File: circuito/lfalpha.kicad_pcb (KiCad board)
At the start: 2 copper layers, 200 x 100 mm, 48 parts, among them J1 BAT, J2 ANALOG, J3 MotorA, J4 MotorB, J5 Bluetooth, J6 REMOTE S/S, J7 SPI, J8 SENSOR CON, J9 SENSOR BAR, SW1 ON/OFF, SW2 START, SW3 STOP, U1 AruinoNano, U2 DRV8835-Carrier, U3 QRE1113, U4 QRE1113, U5 QRE1113, U6 QRE1113, U7 QRE1113, U8 QRE1113

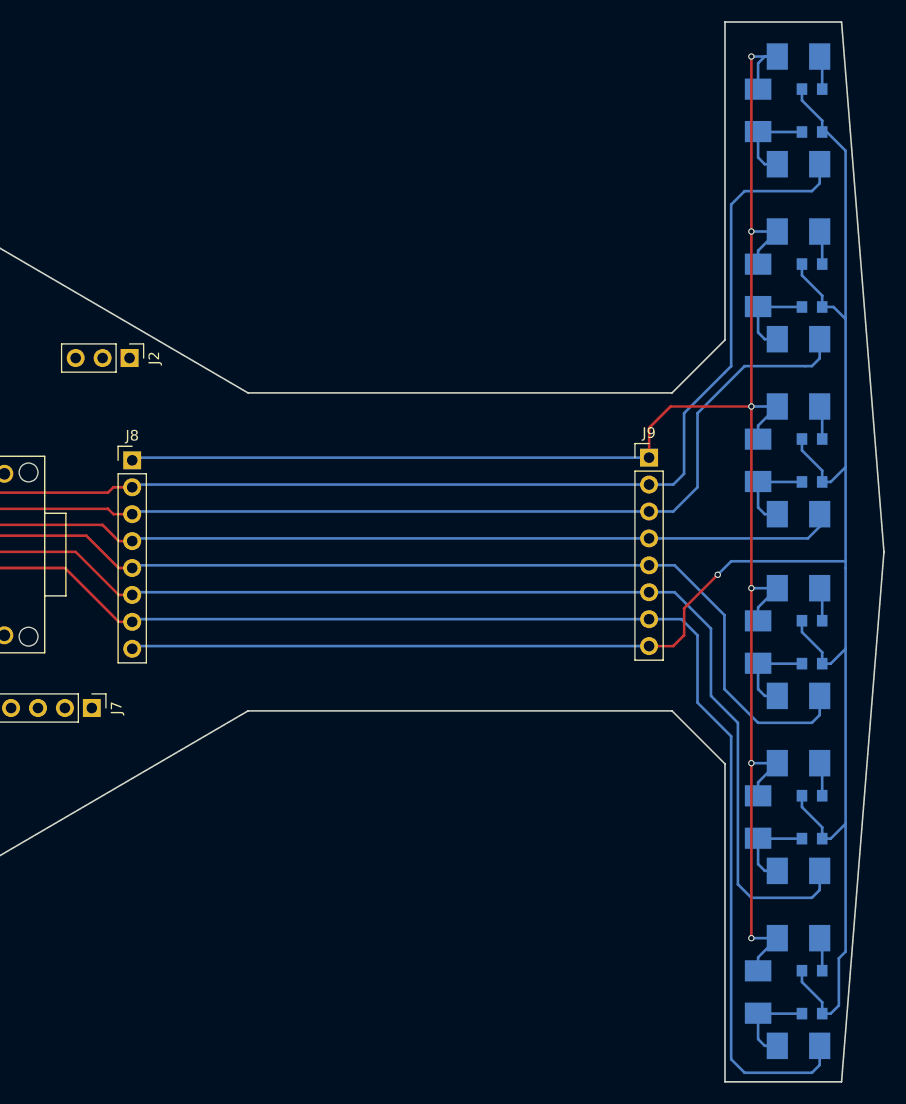
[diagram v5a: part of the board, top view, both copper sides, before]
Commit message: Aggiunto un nuovo Roles per le piste associato alla parte di alimentazione, e ridisegnate alcune piste della barra sensori, ma da completare. Creta l'asola per il ruotino.
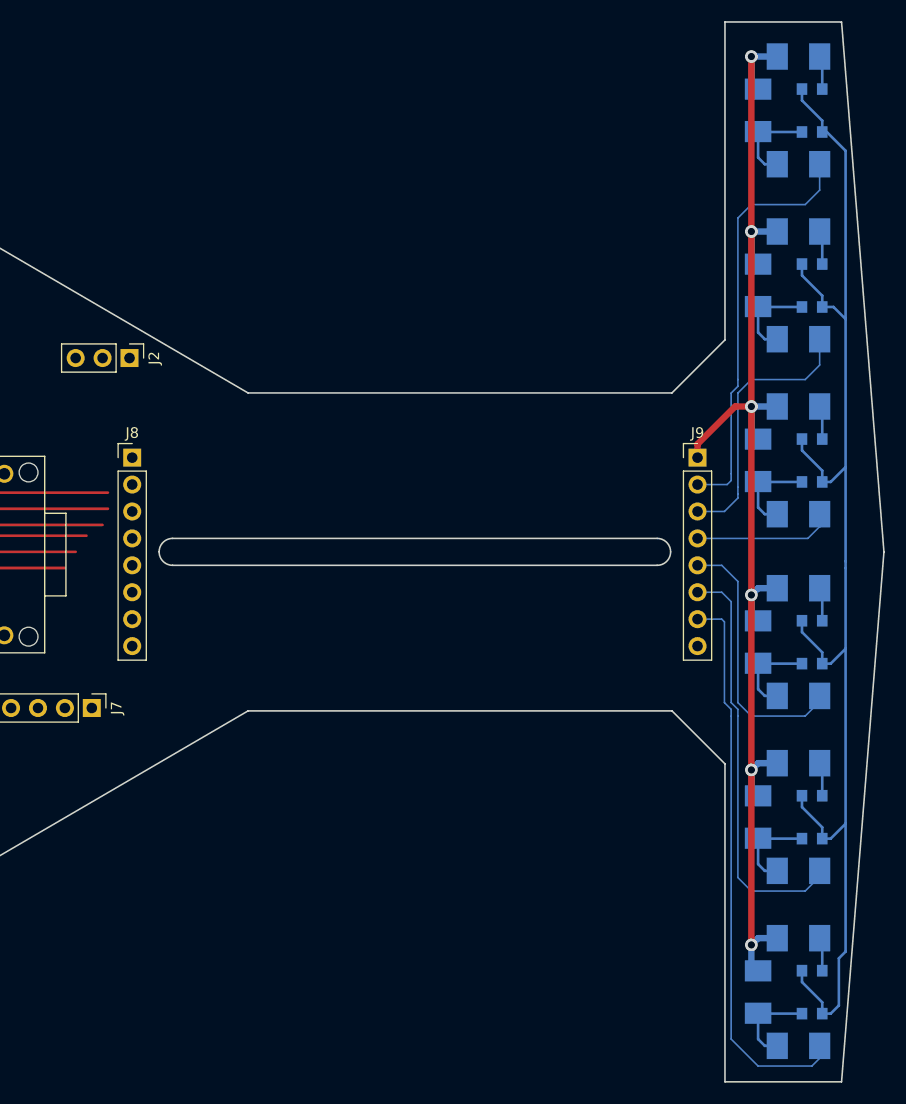
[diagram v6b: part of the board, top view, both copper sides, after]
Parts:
- moved J9 4.57 mm to (232.4, 86.1)
- moved J8 0.25 mm to (179.1, 86.1)
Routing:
- net GND: track 197.7 -> 125.8 mm, vias 1 -> 0
- net Net-(J8-Pad7): track 148.7 -> 87.4 mm
- net Net-(J8-Pad6): track 129.5 -> 70.4 mm
- net +5V: track 183.3 -> 125.3 mm
- net Net-(J8-Pad5): track 110.4 -> 53.1 mm
- net Net-(J8-Pad4): track 95.8 -> 40.5 mm
- net Net-(J8-Pad3): track 101.6 -> 48.1 mm
- net Net-(J8-Pad2): track 111.8 -> 58.4 mm
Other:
- outline, holes or cut-outs redrawn
- net class Alimentazione added: clearance 0.3048, trace_width 0.6096, via_dia 1.1938, via_drill 0.6858

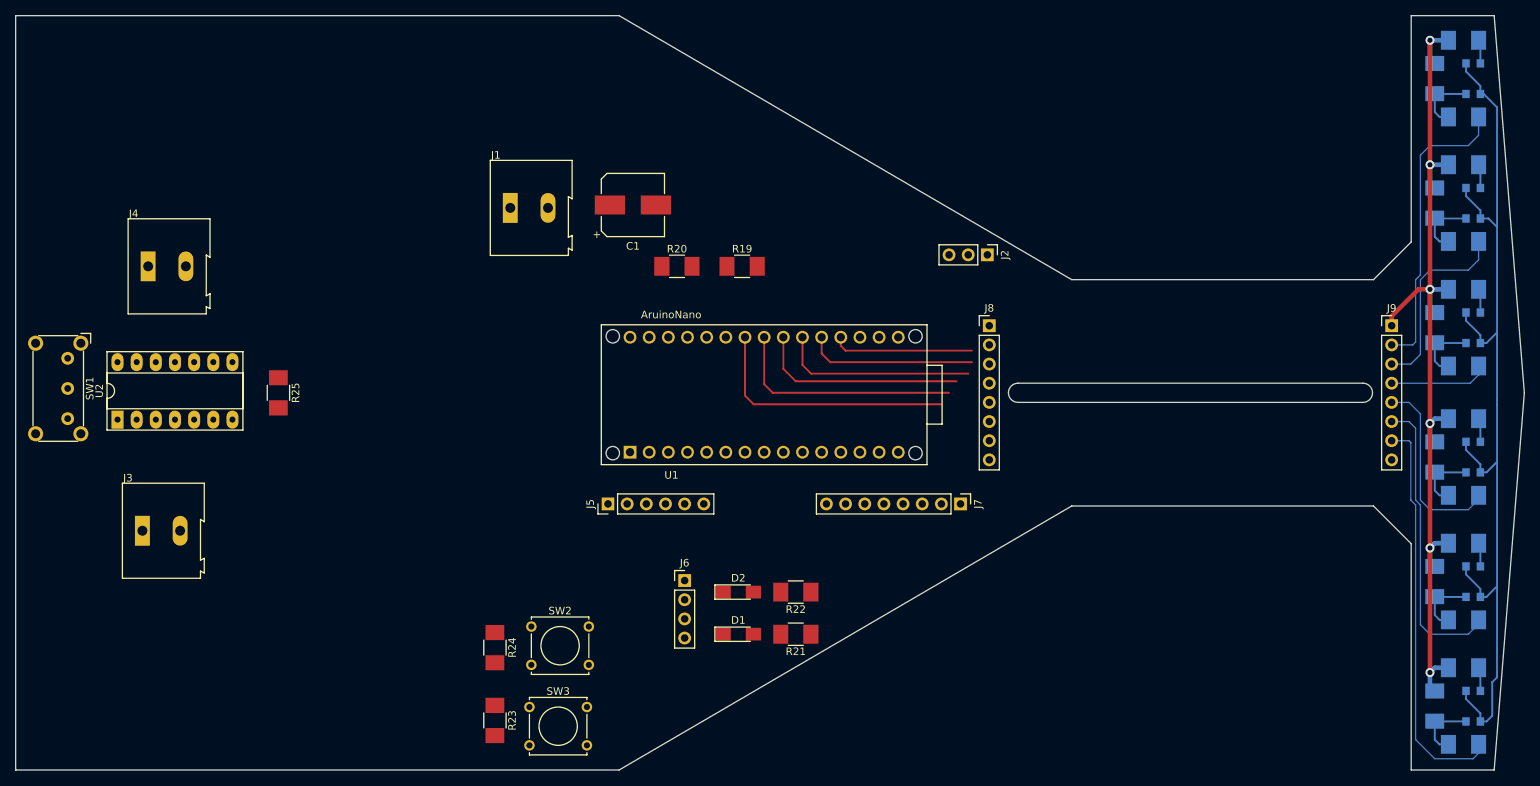
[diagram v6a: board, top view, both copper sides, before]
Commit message: Completate le interconessioni con i sensori e Arduino, piazzati i mount hole per eventuali tagli della barra. Verificare se e come si possono cambiare i connettori attualmente posizionati sulla vista 3D, con altri a 90°
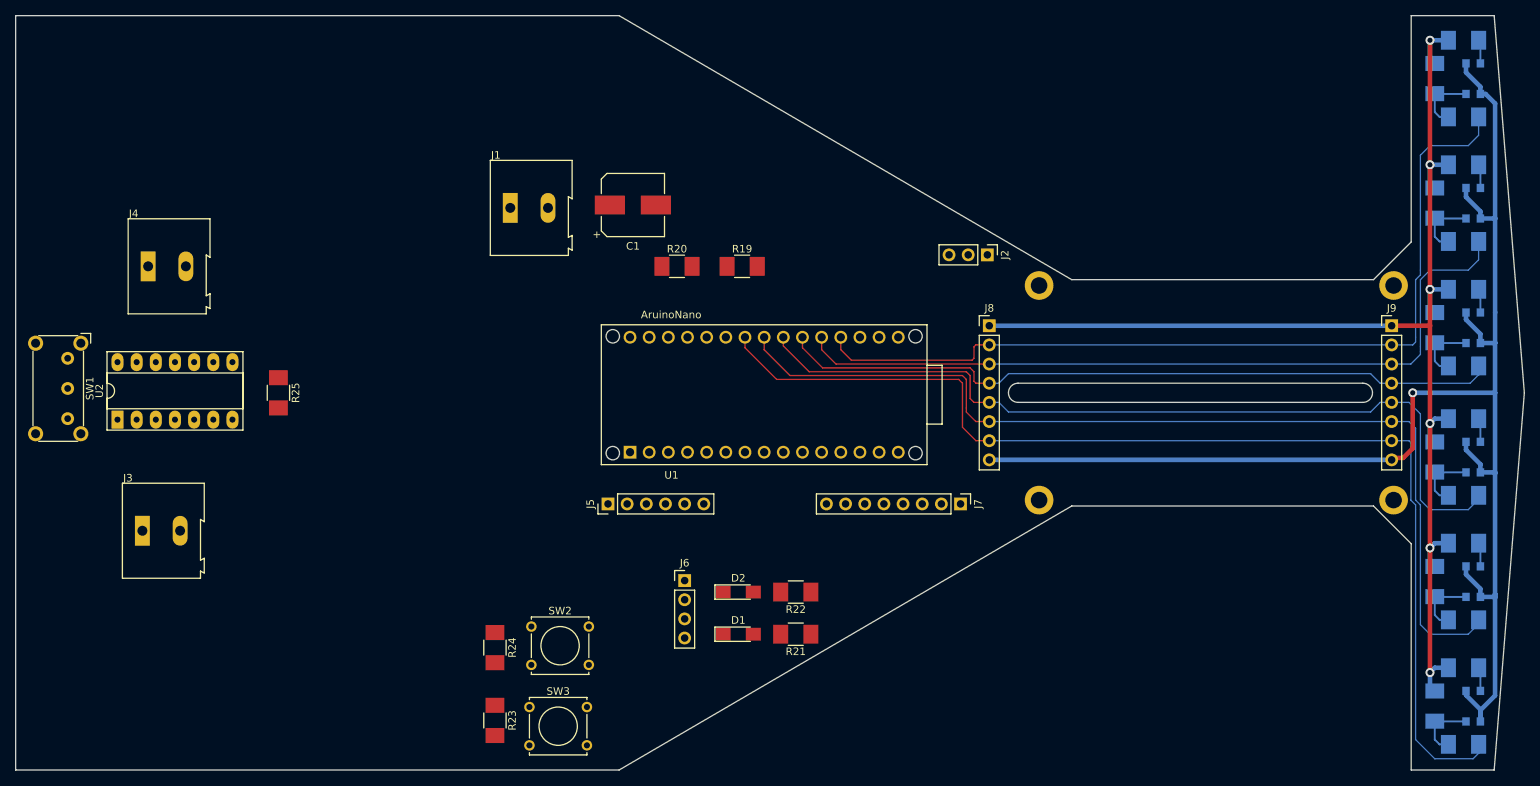
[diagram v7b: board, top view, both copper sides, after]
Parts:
- added REF**: MountingHole_2.2mm_M2_DIN965_Pad, Mounting_Holes:MountingHole_2.2mm_M2_DIN965_Pad, F.Cu at (232.7, 80.8)
- added REF**: MountingHole_2.2mm_M2_DIN965_Pad, Mounting_Holes:MountingHole_2.2mm_M2_DIN965_Pad, F.Cu at (232.7, 109.2)
- added REF**: MountingHole_2.2mm_M2_DIN965_Pad, Mounting_Holes:MountingHole_2.2mm_M2_DIN965_Pad, F.Cu at (185.7, 80.8)
- added REF**: MountingHole_2.2mm_M2_DIN965_Pad, Mounting_Holes:MountingHole_2.2mm_M2_DIN965_Pad, F.Cu at (185.7, 109.2)
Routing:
- net GND: track 125.8 -> 198.3 mm, vias 0 -> 1
- net Net-(J8-Pad7): track 87.4 -> 148.8 mm
- net Net-(J8-Pad6): track 70.4 -> 130.5 mm
- net Net-(J8-Pad5): track 53.1 -> 112.9 mm
- net Net-(J8-Pad2): track 58.4 -> 116.6 mm
- net Net-(J8-Pad4): track 40.5 -> 97.6 mm
- net Net-(J8-Pad3): track 48.1 -> 103.5 mm
- net +5V: track 125.3 -> 175.9 mm

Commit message: Cambiati i connettori strip per avere meno connettori di forma diversa, sistemati alcuni collegamenti per agevolare lo sbroglio. Ridistribuiti connettori e driver motori.
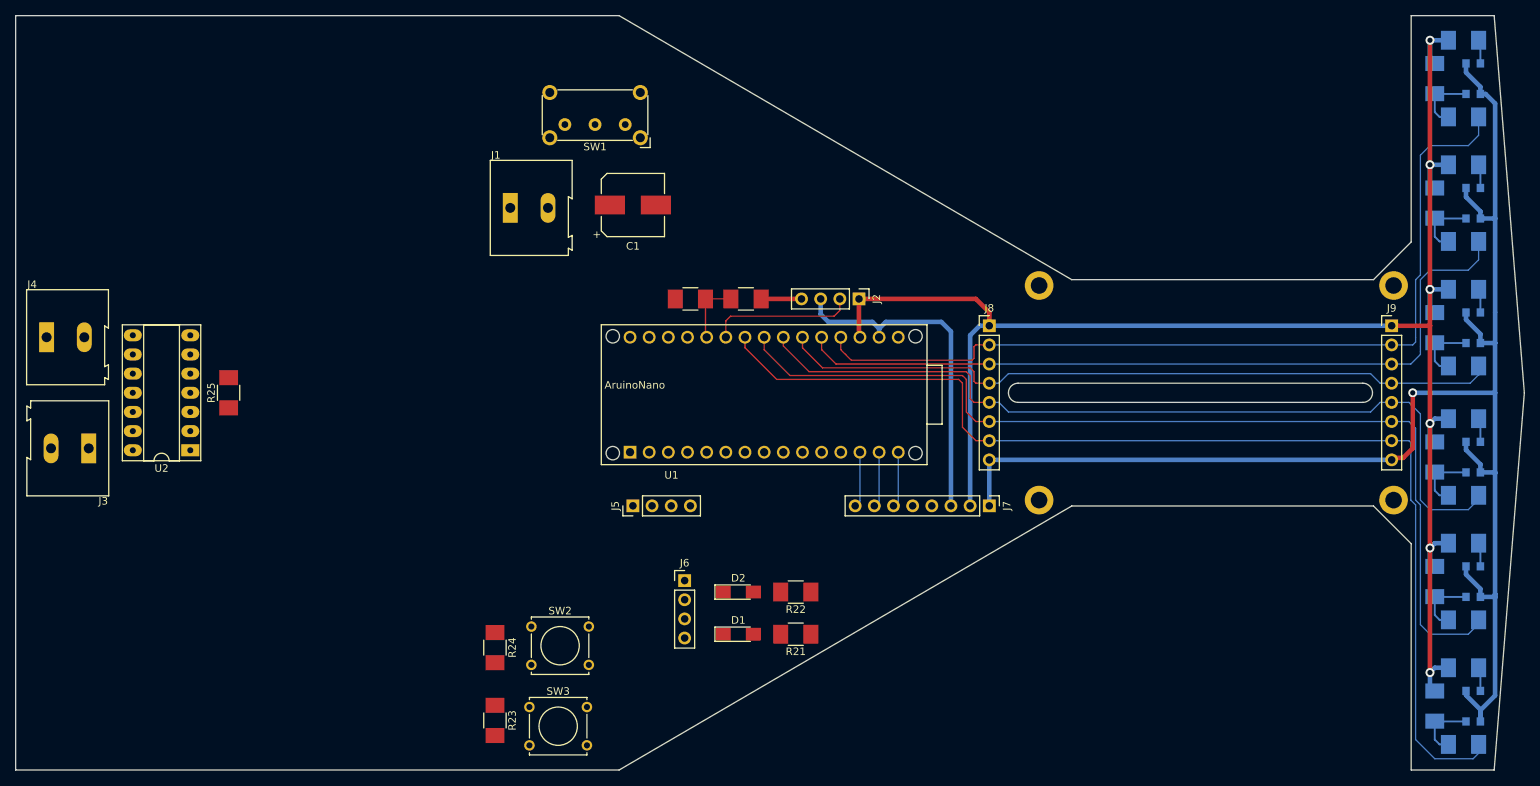
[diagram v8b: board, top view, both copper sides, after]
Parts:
- J2: footprint Socket_Strips:Socket_Strip_Straight_1x03_Pitch2.54mm -> Socket_Strips:Socket_Strip_Straight_1x04_Pitch2.54mm
- J5: footprint Socket_Strips:Socket_Strip_Straight_1x06_Pitch2.54mm -> Socket_Strips:Socket_Strip_Straight_1x04_Pitch2.54mm
- moved SW1 80.1 mm to (130.8, 59.4), turned to 180 degrees
- moved J2 18.0 mm to (161.8, 82.5)
- moved J4 16.4 mm to (54.1, 87.6)
- moved J3 13.0 mm to (59.7, 102.4), turned to 180 degrees
- moved U2 10.5 mm to (73.2, 102.6), turned to 180 degrees
- moved R25 6.60 mm to (78.2, 95.0), turned to 90 degrees
- moved R20 4.67 mm to (139.4, 82.5)
- moved R19 4.35 mm to (146.8, 82.5)
- moved J7 3.82 mm to (179.1, 110.0)
- moved J5 3.31 mm to (131.8, 110.0)
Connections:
- J2 pad 3: GND -> Net-(J2-Pad3)
- J5 pad 3: Net-(J5-Pad3) -> GND
- J5 pad 4: GND -> +5V
- J7 pad 1: +5V -> GND
- J7 pad 2: Net-(J7-Pad2) -> +5V
- J7 pad 3: GND -> Net-(J2-Pad3)
- U1 pad 1: Net-(J5-Pad2) -> Net-(J5-Pad1)
- U1 pad 17: Net-(J7-Pad4) -> Net-(J2-Pad3)
- U1 pad 2: Net-(J5-Pad3) -> Net-(J5-Pad2)
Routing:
- net +5V: track 175.9 -> 226.4 mm
- net Net-(J2-Pad3): track 0.00 -> 45.2 mm
- net Net-(J2-Pad2): track 0.00 -> 19.4 mm
- net GND: track 198.3 -> 209.7 mm
- net Net-(R19-Pad1): track 0.00 -> 8.51 mm
- net Net-(J7-Pad8): track 0.00 -> 7.38 mm
- net Net-(J7-Pad7): track 0.00 -> 7.38 mm
- net Net-(J7-Pad6): track 0.00 -> 7.38 mm
